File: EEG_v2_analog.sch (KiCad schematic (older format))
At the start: 37 parts, among them J1 BIAS, J10 IN5P, J11 IN5N, J12 IN6P, J13 IN6N, J14 IN7P, J15 IN7N, J16 IN8P, J17 IN8N, J18 SRB1, J19 SRB2, J2 IN1P, J3 IN1N, J4 IN2P, J5 IN2N, J6 IN3P, J7 IN3N, J8 IN4P, J9 IN4N, U1 ADS1299IPAGR

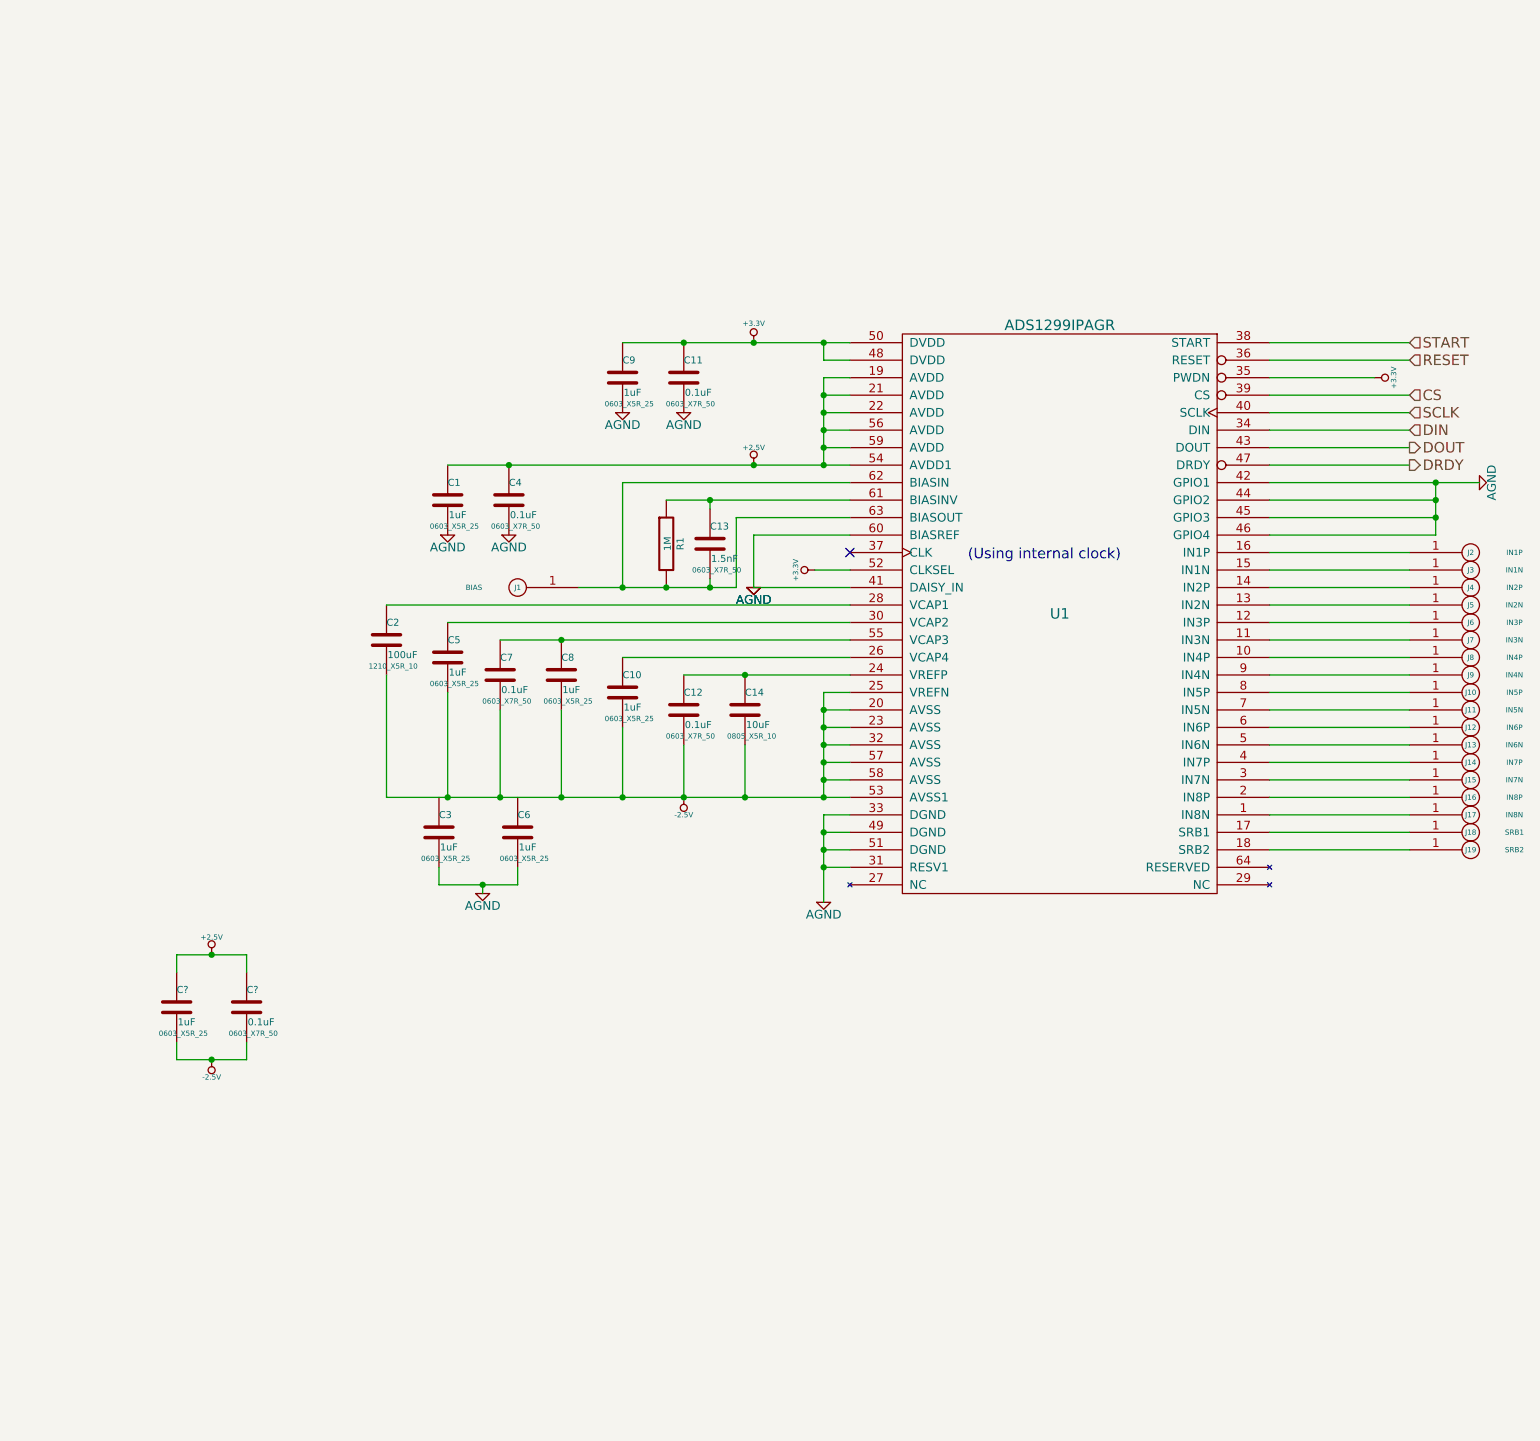
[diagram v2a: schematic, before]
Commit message: Clean ERC errors.
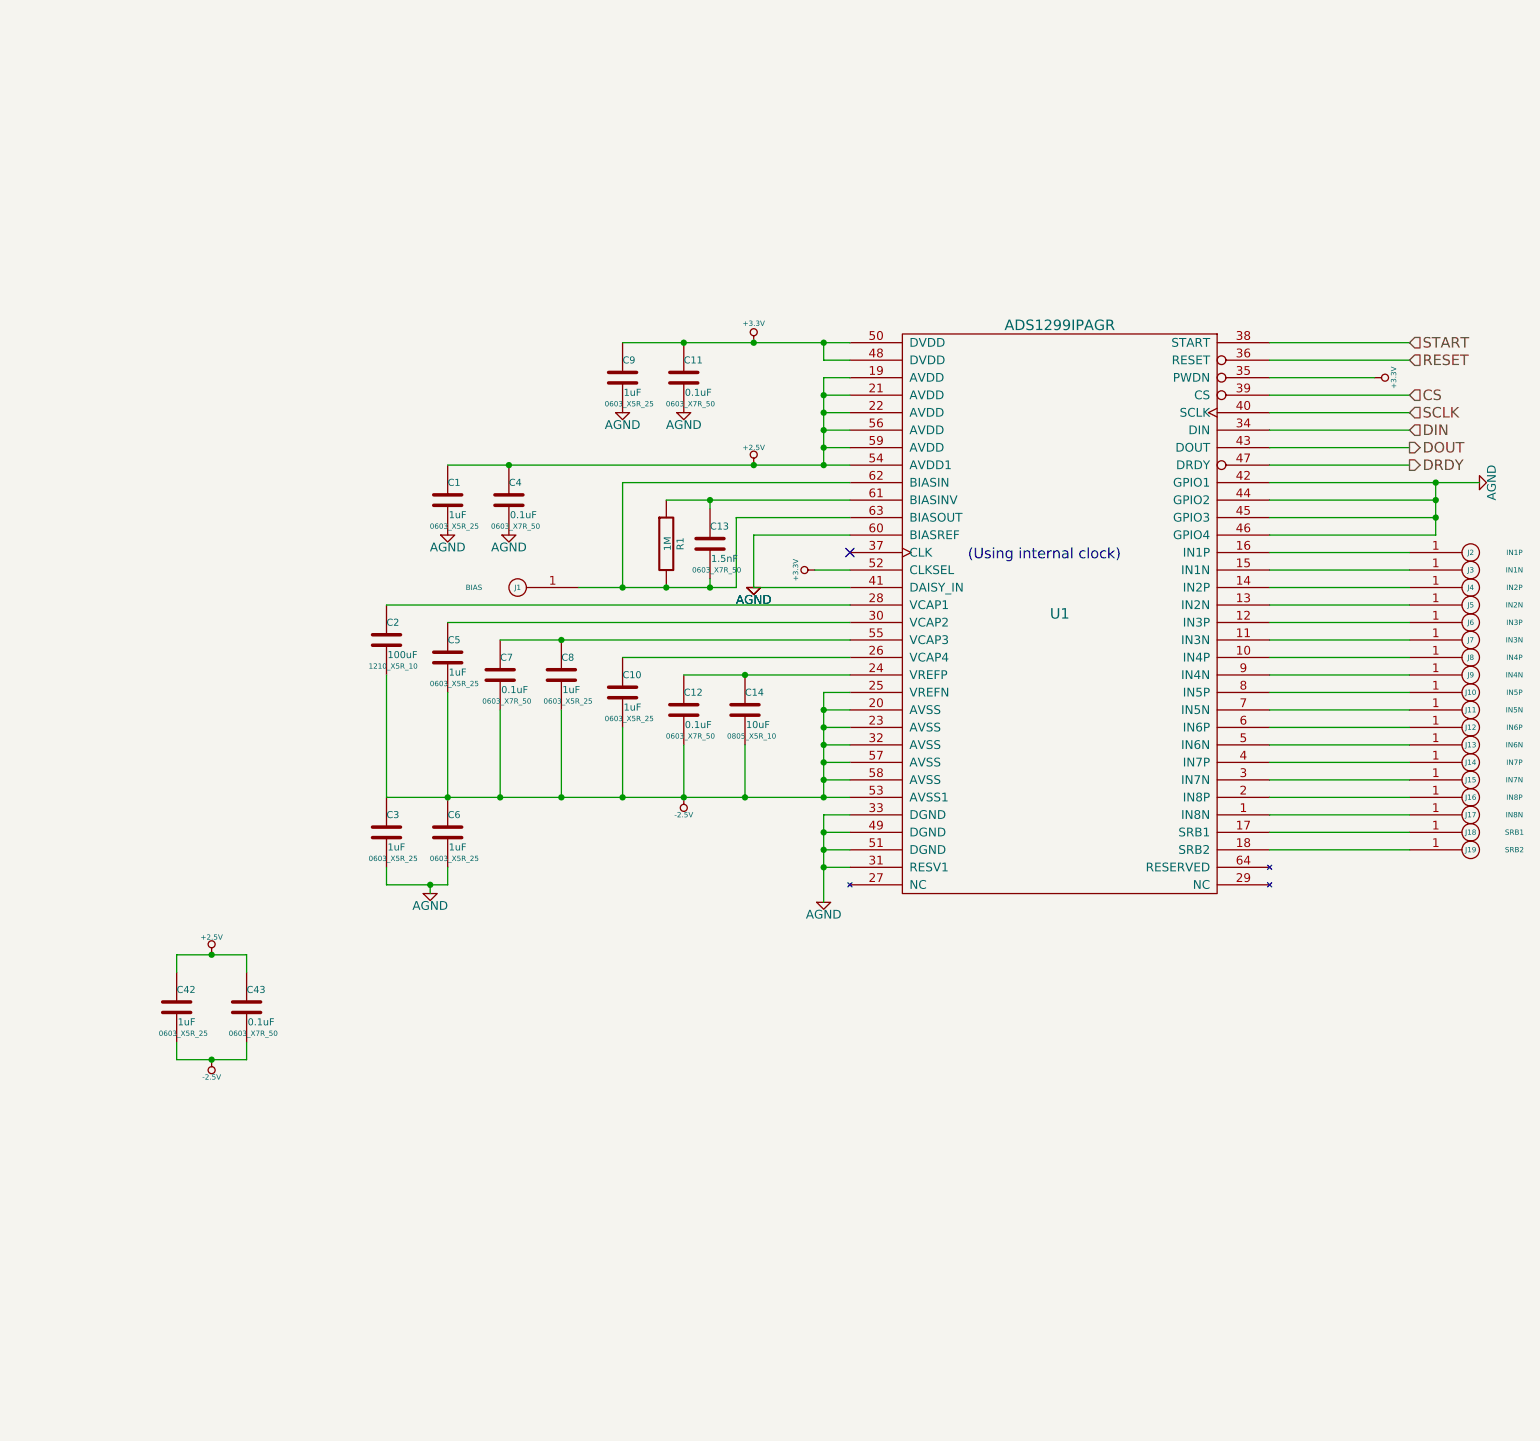
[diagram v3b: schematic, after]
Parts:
- gave numbers to parts that had none: 2
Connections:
- net -2.5V: now also C3.1, C6.1
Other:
- moved on the sheet: C3, C6
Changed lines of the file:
@@
 L C C3
 U 1 1 54B45DFE
-P 2950 5300
-F 0 "C3" H 2950 5400 40  0000 L CNN
-F 1 "1uF" H 2956 5215 40  0000 L CNN
-F 2 "0603_X5R_25" H 2988 5150 30  0000 C CNN
-F 3 "~" H 2950 5300 60  0000 C CNN
-	1    2950 5300
+P 2650 5300
+F 0 "C3" H 2650 5400 40  0000 L CNN
+F 1 "1uF" H 2656 5215 40  0000 L CNN
+F 2 "0603_X5R_25" H 2688 5150 30  0000 C CNN
+F 3 "~" H 2650 5300 60  0000 C CNN
+	1    2650 5300
 	1    0    0    -1
 $EndComp
@@
 L C C6
 U 1 1 54B45E04
-P 3400 5300
-F 0 "C6" H 3400 5400 40  0000 L CNN
-F 1 "1uF" H 3406 5215 40  0000 L CNN
-F 2 "0603_X5R_25" H 3438 5150 30  0000 C CNN
-F 3 "~" H 3400 5300 60  0000 C CNN
-	1    3400 5300
+P 3000 5300
+F 0 "C6" H 3000 5400 40  0000 L CNN
+F 1 "1uF" H 3006 5215 40  0000 L CNN
+F 2 "0603_X5R_25" H 3038 5150 30  0000 C CNN
+F 3 "~" H 3000 5300 60  0000 C CNN
+	1    3000 5300
 	1    0    0    -1
 $EndComp
@@
 L AGND #PWR08
 U 1 1 54B45E0A
-P 3200 5650
-F 0 "#PWR08" H 3200 5650 40  0001 C CNN
-F 1 "AGND" H 3200 5580 50  0000 C CNN
-F 2 "" H 3200 5650 60  0000 C CNN
-F 3 "" H 3200 5650 60  0000 C CNN
-	1    3200 5650
+P 2900 5650
+F 0 "#PWR08" H 2900 5650 40  0001 C CNN
+F 1 "AGND" H 2900 5580 50  0000 C CNN
+F 2 "" H 2900 5650 60  0000 C CNN
+F 3 "" H 2900 5650 60  0000 C CNN
+	1    2900 5650
 	1    0    0    -1
 $EndComp
@@
 	7700 3500 8650 3500
 Wire Wire Line
-	7700 3600 8650 3600
+	8650 3600 7700 3600
 Wire Wire Line
 	8500 3700 7700 3700
@@
 	4750 3600 4750 3900
 Wire Wire Line
-	2950 5500 2950 5600
-Wire Wire Line
-	2950 5600 3400 5600
-Wire Wire Line
-	3200 5600 3200 5650
-Wire Wire Line
-	3400 5600 3400 5500
-Connection ~ 3200 5600
-$Comp
-L AGND #PWR?
+	2650 5500 2650 5600
+Wire Wire Line
+	2650 5600 3000 5600
+Wire Wire Line
+	2900 5600 2900 5650
+Wire Wire Line
+	3000 5600 3000 5500
+Connection ~ 2900 5600
+$Comp
+L AGND #PWR017
 U 1 1 54C4ED9D
 P 8900 3300
-F 0 "#PWR?" H 8900 3300 40  0001 C CNN
+F 0 "#PWR017" H 8900 3300 40  0001 C CNN
 F 1 "AGND" H 8900 3230 50  0000 C CNN
 F 2 "" H 8900 3300 60  0000 C CNN
@@
 $EndComp
 Wire Wire Line
-	8650 3600 8650 3300
+	8650 3300 8650 3600
 Connection ~ 8650 3300
 Connection ~ 8650 3400
 Connection ~ 8650 3500
 $Comp
-L C C?
+L C C43
 U 1 1 54C4F289
 P 1850 6300
-F 0 "C?" H 1850 6400 40  0000 L CNN
+F 0 "C43" H 1850 6400 40  0000 L CNN
 F 1 "0.1uF" H 1856 6215 40  0000 L CNN
 F 2 "0603_X7R_50" H 1888 6150 30  0000 C CNN
@@
 $EndComp
 $Comp
-L C C?
+L C C42
 U 1 1 54C4F28F
 P 1450 6300
-F 0 "C?" H 1450 6400 40  0000 L CNN
+F 0 "C42" H 1450 6400 40  0000 L CNN
 F 1 "1uF" H 1456 6215 40  0000 L CNN
 F 2 "0603_X5R_25" H 1488 6150 30  0000 C CNN
@@
 $EndComp
 $Comp
-L -2.5V #PWR?
+L -2.5V #PWR018
 U 1 1 54C4F2A1
 P 1650 6600
-F 0 "#PWR?" H 1650 6550 20  0001 C CNN
+F 0 "#PWR018" H 1650 6550 20  0001 C CNN
 F 1 "-2.5V" H 1650 6700 30  0000 C CNN
 F 2 "" H 1650 6600 60  0000 C CNN
@@
 $EndComp
 $Comp
-L +2.5V #PWR?
+L +2.5V #PWR019
 U 1 1 54C4F2B1
 P 1650 6000
-F 0 "#PWR?" H 1650 5950 20  0001 C CNN
+F 0 "#PWR019" H 1650 5950 20  0001 C CNN
 F 1 "+2.5V" H 1650 6100 30  0000 C CNN
 F 2 "" H 1650 6000 60  0000 C CNN

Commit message: Added patient protection resistors and filter caps to input electroes
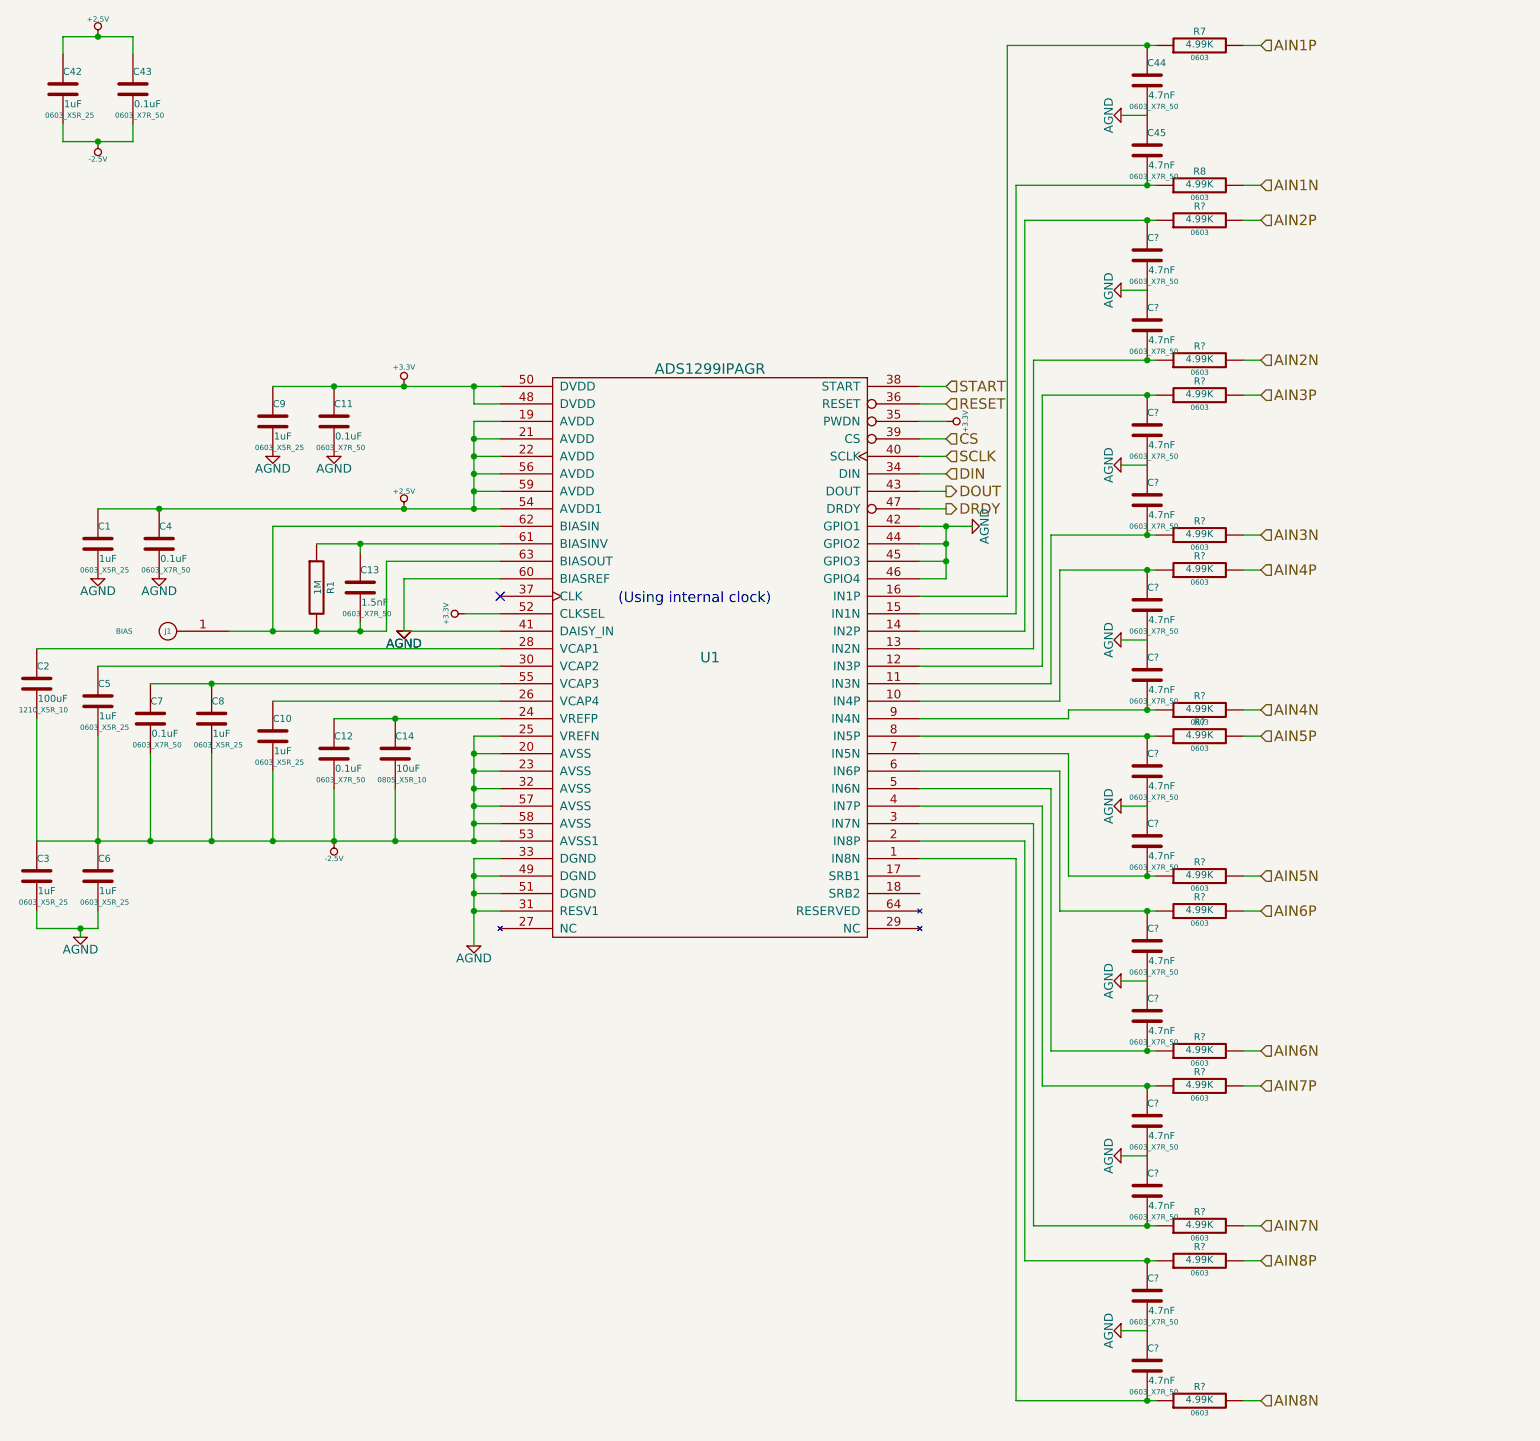
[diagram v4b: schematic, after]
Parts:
- removed J10: IN5P, ~, symbol SMD_1PIN_PAD
- removed J11: IN5N, ~, symbol SMD_1PIN_PAD
- removed J12: IN6P, ~, symbol SMD_1PIN_PAD
- removed J13: IN6N, ~, symbol SMD_1PIN_PAD
- removed J14: IN7P, ~, symbol SMD_1PIN_PAD
- removed J15: IN7N, ~, symbol SMD_1PIN_PAD
- removed J16: IN8P, ~, symbol SMD_1PIN_PAD
- removed J17: IN8N, ~, symbol SMD_1PIN_PAD
- removed J18: SRB1, ~, symbol SMD_1PIN_PAD
- removed J19: SRB2, ~, symbol SMD_1PIN_PAD
- removed J2: IN1P, ~, symbol SMD_1PIN_PAD
- removed J3: IN1N, ~, symbol SMD_1PIN_PAD
- removed J4: IN2P, ~, symbol SMD_1PIN_PAD
- removed J5: IN2N, ~, symbol SMD_1PIN_PAD
- removed J6: IN3P, ~, symbol SMD_1PIN_PAD
- removed J7: IN3N, ~, symbol SMD_1PIN_PAD
- removed J8: IN4P, ~, symbol SMD_1PIN_PAD
- removed J9: IN4N, ~, symbol SMD_1PIN_PAD
- added C44, C45, C? (x14): 4.7nF, 0603_X7R_50, symbol C
- added R7, R8, R? (x14): 4.99K, 0603, symbol R
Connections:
- net AGND: now also C44.2, C45.1, C?.1, C?.1, C?.1, C?.1, C?.1, C?.1, C?.1, C?.2, C?.2, C?.2, C?.2, C?.2, C?.2, C?.2
- net at U1.1 (IN8N): now also C?.2, R?.1
- net at U1.10 (IN4P): now also C?.1, R?.1
- net at U1.11 (IN3N): now also C?.2, R?.1
- net at U1.12 (IN3P): now also C?.1, R?.1
- net at U1.13 (IN2N): now also C?.2, R?.1
- net at U1.14 (IN2P): now also C?.1, R?.1
- net at U1.15 (IN1N): now also C45.2, R8.1
- net at U1.16 (IN1P): now also C44.1, R7.1
- net at U1.2 (IN8P): now also C?.1, R?.1
- net at U1.3 (IN7N): now also C?.2, R?.1
- net at U1.4 (IN7P): now also C?.1, R?.1
- net at U1.5 (IN6N): now also C?.2, R?.1
- net at U1.6 (IN6P): now also C?.1, R?.1
- net at U1.7 (IN5N): now also C?.2, R?.1
- net at U1.8 (IN5P): now also C?.1, R?.1
- net at U1.9 (IN4N): now also C?.2, R?.1
- new net AIN1N: R8.2
- new net AIN1P: R7.2
- new net AIN2N: R?.2
- new net AIN2P: R?.2
- new net AIN3N: R?.2
- new net AIN3P: R?.2
- new net AIN4N: R?.2
- new net AIN4P: R?.2
- new net AIN5N: R?.2
- new net AIN5P: R?.2
- new net AIN6N: R?.2
- new net AIN6P: R?.2
- new net AIN7N: R?.2
- new net AIN7P: R?.2
- new net AIN8N: R?.2
- new net AIN8P: R?.2
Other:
- moved on the sheet: C1, C10, C11, C12, C13, C14, C2, C3, C4, C42, C43, C5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
